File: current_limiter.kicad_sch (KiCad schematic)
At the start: 22 parts, among them J3601 Conn_02x02, Q3601 MMBT5551, Q3602 MMBT5551, Q3603 LBSS84LT1G, U3601 COS1333TR, U3602 LMV321-TR

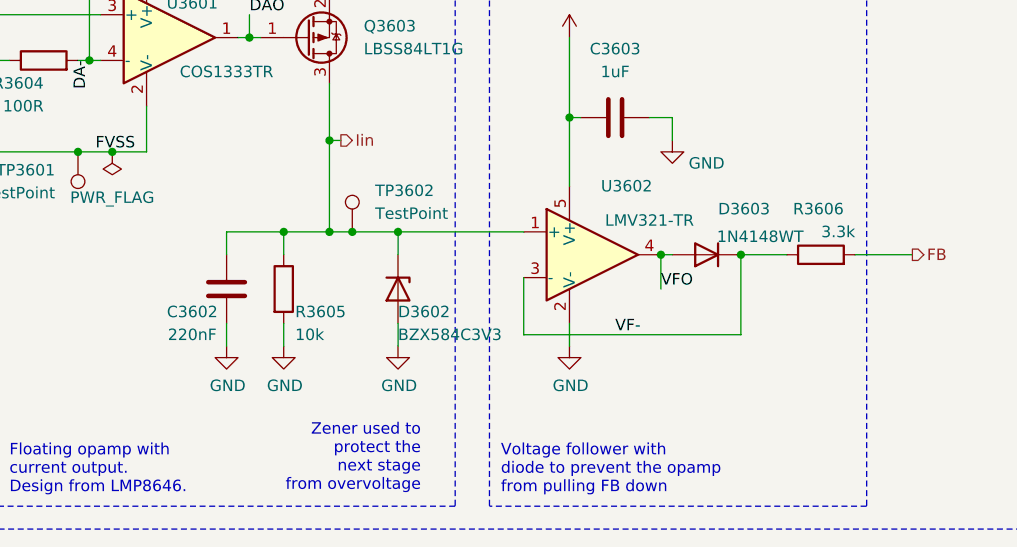
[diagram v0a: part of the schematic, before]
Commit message: Update current limiter components
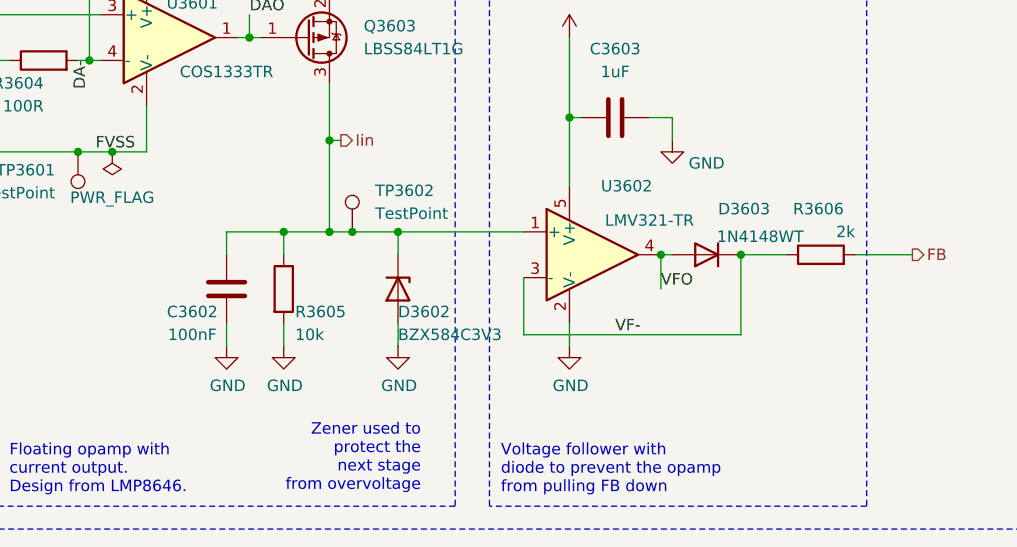
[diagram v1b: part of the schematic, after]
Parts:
- C3602: value 220nF -> 100nF; LCSC C21120 -> (none)
- R3605: footprint Resistor_SMD:R_0402_1005Metric -> Resistor_SMD:R_0603_1608Metric_Pad0.98x0.95mm_HandSolder; LCSC C25744 -> (none)
- R3606: value 3.3k -> 2k; LCSC C22978 -> (none)
- R3607: footprint Resistor_SMD:R_0402_1005Metric -> Resistor_SMD:R_0603_1608Metric_Pad0.98x0.95mm_HandSolder; LCSC C25918 -> (none)
- R3608: footprint Resistor_SMD:R_0402_1005Metric -> Resistor_SMD:R_0603_1608Metric_Pad0.98x0.95mm_HandSolder; LCSC C51721 -> (none)
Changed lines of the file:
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@@
 			)
 		)
-		(property "Footprint" "Resistor_SMD:R_0402_1005Metric"
+		(property "Footprint" "Resistor_SMD:R_0603_1608Metric_Pad0.98x0.95mm_HandSolder"
 			(at 113.792 99.06 90)
 			(effects
@@
 			)
 		)
-		(property "LCSC" "C25744"
+		(property "LCSC" ""
 			(at 115.57 99.06 0)
 			(effects
@@
 			)
 		)
-		(property "Value" "220nF"
+		(property "Value" "100nF"
 			(at 105.41 104.14 0)
 			(effects
@@
 			)
 		)
-		(property "LCSC" "C21120"
+		(property "LCSC" ""
 			(at 109.22 99.06 0)
 			(effects
@@
 			)
 		)
-		(property "Footprint" "Resistor_SMD:R_0402_1005Metric"
+		(property "Footprint" "Resistor_SMD:R_0603_1608Metric_Pad0.98x0.95mm_HandSolder"
 			(at 228.6 97.79 0)
 			(effects
@@
 			)
 		)
-		(property "LCSC" "C25918"
+		(property "LCSC" ""
 			(at 228.6 97.79 0)
 			(effects
@@
 			)
 		)
-		(property "Value" "3.3k"
+		(property "Value" "2k"
 			(at 179.07 92.71 90)
 			(effects
@@
 			)
 		)
-		(property "LCSC" "C22978"
+		(property "LCSC" ""
 			(at 175.26 95.25 0)
 			(effects
@@
 			)
 		)
-		(property "Footprint" "Resistor_SMD:R_0402_1005Metric"
+		(property "Footprint" "Resistor_SMD:R_0603_1608Metric_Pad0.98x0.95mm_HandSolder"
 			(at 241.3 97.79 0)
 			(effects
@@
 			)
 		)
-		(property "LCSC" "C51721"
+		(property "LCSC" ""
 			(at 241.3 97.79 0)
 			(effects

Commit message: Try to improve current limiter stability
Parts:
- C167: renamed from C3602; LCSC (none) -> C14663
- R116: renamed from R3605; LCSC (none) -> C25804
- R117: renamed from R3606; LCSC (none) -> C22975
- R118: renamed from R3607; LCSC (none) -> C23234
- R119: renamed from R3608; LCSC (none) -> C23018
- renumbered C3601 to C166, C3603 to C168, D3601 to D38, D3602 to D39, D3603 to D40, J3601 to J31, Q3602 to Q10, Q3603 to Q11, Q3601 to Q9, R3601 to R112, R3602 to R113, R3603 to R114, R3604 to R115, TP3601 to TP43, TP3602 to TP44, U3601 to U52, U3602 to U53

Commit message: Reannotate the board
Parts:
- renumbered C166 to C167, C167 to C168, C168 to C169, D38 to D37, D39 to D38, D40 to D39, J31 to J30, TP43 to TP42, TP44 to TP43, U52 to U51, U53 to U52
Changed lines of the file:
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@@
 		(on_board yes)
 		(dnp no)
-		(property "Reference" "J31"
+		(property "Reference" "J30"
 			(at 246.634 78.994 0)
 			(effects
@@
 			(project "HALPI2"
 				(path "/abc482bd-3f17-4d35-80db-1da3dcdb5c27/c7bf4e1f-6bd1-4be7-9e56-1bd438bf5d42/949897e8-9bb6-4c13-b9c6-3f831f2e4c69/ceedefa9-b0a1-435b-ac8f-bf0512726438"
-					(reference "J31")
+					(reference "J30")
 					(unit 1)
 				)
@@
 		(on_board yes)
 		(dnp no)
-		(property "Reference" "D40"
+		(property "Reference" "D39"
 			(at 163.83 90.17 0)
 			(effects
@@
 			(project "HALPI2"
 				(path "/abc482bd-3f17-4d35-80db-1da3dcdb5c27/c7bf4e1f-6bd1-4be7-9e56-1bd438bf5d42/949897e8-9bb6-4c13-b9c6-3f831f2e4c69/ceedefa9-b0a1-435b-ac8f-bf0512726438"
-					(reference "D40")
+					(reference "D39")
 					(unit 1)
 				)
@@
 		(dnp no)
 		(fields_autoplaced yes)
-		(property "Reference" "C168"
+		(property "Reference" "C169"
 			(at 152.4 72.39 90)
 			(effects
@@
 			(project "HALPI2"
 				(path "/abc482bd-3f17-4d35-80db-1da3dcdb5c27/c7bf4e1f-6bd1-4be7-9e56-1bd438bf5d42/949897e8-9bb6-4c13-b9c6-3f831f2e4c69/ceedefa9-b0a1-435b-ac8f-bf0512726438"
-					(reference "C168")
+					(reference "C169")
 					(unit 1)
 				)
@@
 		(dnp no)
 		(fields_autoplaced yes)
-		(property "Reference" "D38"
+		(property "Reference" "D37"
 			(at 71.12 78.7399 90)
 			(effects
@@
 			(project "HALPI2"
 				(path "/abc482bd-3f17-4d35-80db-1da3dcdb5c27/c7bf4e1f-6bd1-4be7-9e56-1bd438bf5d42/949897e8-9bb6-4c13-b9c6-3f831f2e4c69/ceedefa9-b0a1-435b-ac8f-bf0512726438"
-					(reference "D38")
+					(reference "D37")
 					(unit 1)
 				)
@@
 		(on_board yes)
 		(dnp no)
-		(property "Reference" "#PWR0324"
+		(property "Reference" "#PWR0323"
 			(at 158.75 88.9 0)
 			(effects
@@
 			(project "HALPI2"
 				(path "/abc482bd-3f17-4d35-80db-1da3dcdb5c27/c7bf4e1f-6bd1-4be7-9e56-1bd438bf5d42/949897e8-9bb6-4c13-b9c6-3f831f2e4c69/ceedefa9-b0a1-435b-ac8f-bf0512726438"
-					(reference "#PWR0324")
+					(reference "#PWR0323")
 					(unit 1)
 				)
@@
 		(on_board yes)
 		(dnp no)
-		(property "Reference" "#PWR0321"
+		(property "Reference" "#PWR0320"
 			(at 128.27 111.76 0)
 			(effects
@@
 			(project "HALPI2"
 				(path "/abc482bd-3f17-4d35-80db-1da3dcdb5c27/c7bf4e1f-6bd1-4be7-9e56-1bd438bf5d42/949897e8-9bb6-4c13-b9c6-3f831f2e4c69/ceedefa9-b0a1-435b-ac8f-bf0512726438"
-					(reference "#PWR0321")
+					(reference "#PWR0320")
 					(unit 1)
 				)
@@
 		(on_board yes)
 		(dnp no)
-		(property "Reference" "#PWR0320"
+		(property "Reference" "#PWR0319"
 			(at 115.57 111.76 0)
 			(effects
@@
 			(project "HALPI2"
 				(path "/abc482bd-3f17-4d35-80db-1da3dcdb5c27/c7bf4e1f-6bd1-4be7-9e56-1bd438bf5d42/949897e8-9bb6-4c13-b9c6-3f831f2e4c69/ceedefa9-b0a1-435b-ac8f-bf0512726438"
-					(reference "#PWR0320")
+					(reference "#PWR0319")
 					(unit 1)
 				)
@@
 		(dnp no)
 		(fields_autoplaced yes)
-		(property "Reference" "#PWR0325"
+		(property "Reference" "#PWR0324"
 			(at 228.6 111.76 0)
 			(effects
@@
 			(project "HALPI2"
 				(path "/abc482bd-3f17-4d35-80db-1da3dcdb5c27/c7bf4e1f-6bd1-4be7-9e56-1bd438bf5d42/949897e8-9bb6-4c13-b9c6-3f831f2e4c69/ceedefa9-b0a1-435b-ac8f-bf0512726438"
-					(reference "#PWR0325")
+					(reference "#PWR0324")
 					(unit 1)
 				)
@@
 		(on_board yes)
 		(dnp no)
-		(property "Reference" "C167"
+		(property "Reference" "C168"
 			(at 105.41 101.6 0)
 			(effects
@@
 			(project "HALPI2"
 				(path "/abc482bd-3f17-4d35-80db-1da3dcdb5c27/c7bf4e1f-6bd1-4be7-9e56-1bd438bf5d42/949897e8-9bb6-4c13-b9c6-3f831f2e4c69/ceedefa9-b0a1-435b-ac8f-bf0512726438"
-					(reference "C167")
+					(reference "C168")
 					(unit 1)
 				)
@@
 		(on_board yes)
 		(dnp no)
-		(property "Reference" "#PWR0323"
+		(property "Reference" "#PWR0322"
 			(at 147.32 111.76 0)
 			(effects
@@
 			(project "HALPI2"
 				(path "/abc482bd-3f17-4d35-80db-1da3dcdb5c27/c7bf4e1f-6bd1-4be7-9e56-1bd438bf5d42/949897e8-9bb6-4c13-b9c6-3f831f2e4c69/ceedefa9-b0a1-435b-ac8f-bf0512726438"
-					(reference "#PWR0323")
+					(reference "#PWR0322")
 					(unit 1)
 				)
@@
 		(dnp no)
 		(fields_autoplaced yes)
-		(property "Reference" "#PWR0326"
+		(property "Reference" "#PWR0325"
 			(at 241.3 111.76 0)
 			(effects
@@
 			(project "HALPI2"
 				(path "/abc482bd-3f17-4d35-80db-1da3dcdb5c27/c7bf4e1f-6bd1-4be7-9e56-1bd438bf5d42/949897e8-9bb6-4c13-b9c6-3f831f2e4c69/ceedefa9-b0a1-435b-ac8f-bf0512726438"
-					(reference "#PWR0326")
+					(reference "#PWR0325")
 					(unit 1)
 				)
@@
 		(on_board yes)
 		(dnp no)
-		(property "Reference" "TP43"
+		(property "Reference" "TP42"
 			(at 90.17 85.8519 0)
 			(effects
@@
 			(project "HALPI2"
 				(path "/abc482bd-3f17-4d35-80db-1da3dcdb5c27/c7bf4e1f-6bd1-4be7-9e56-1bd438bf5d42/949897e8-9bb6-4c13-b9c6-3f831f2e4c69/ceedefa9-b0a1-435b-ac8f-bf0512726438"
-					(reference "TP43")
+					(reference "TP42")
 					(unit 1)
 				)
@@
 		(on_board yes)
 		(dnp no)
-		(property "Reference" "#PWR0319"
+		(property "Reference" "#PWR0318"
 			(at 109.22 111.76 0)
 			(effects
@@
 			(project "HALPI2"
 				(path "/abc482bd-3f17-4d35-80db-1da3dcdb5c27/c7bf4e1f-6bd1-4be7-9e56-1bd438bf5d42/949897e8-9bb6-4c13-b9c6-3f831f2e4c69/ceedefa9-b0a1-435b-ac8f-bf0512726438"
-					(reference "#PWR0319")
+					(reference "#PWR0318")
 					(unit 1)
 				)
@@
 		(dnp no)
 		(fields_autoplaced yes)
-		(property "Reference" "TP44"
+		(property "Reference" "TP43"
 			(at 125.73 88.1379 0)
 			(effects
@@
 			(project "HALPI2"
 				(path "/abc482bd-3f17-4d35-80db-1da3dcdb5c27/c7bf4e1f-6bd1-4be7-9e56-1bd438bf5d42/949897e8-9bb6-4c13-b9c6-3f831f2e4c69/ceedefa9-b0a1-435b-ac8f-bf0512726438"
-					(reference "TP44")
+					(reference "TP43")
 					(unit 1)
 				)
@@
 		(dnp no)
 		(fields_autoplaced yes)
-		(property "Reference" "#FLG023"
+		(property "Reference" "#FLG022"
 			(at 91.44 55.245 0)
 			(effects
@@
 			(project "HALPI2"
 				(path "/abc482bd-3f17-4d35-80db-1da3dcdb5c27/c7bf4e1f-6bd1-4be7-9e56-1bd438bf5d42/949897e8-9bb6-4c13-b9c6-3f831f2e4c69/ceedefa9-b0a1-435b-ac8f-bf0512726438"
-					(reference "#FLG023")
+					(reference "#FLG022")
 					(unit 1)
 				)
@@
 		(dnp no)
 		(fields_autoplaced yes)
-		(property "Reference" "#PWR0322"
+		(property "Reference" "#PWR0321"
 			(at 147.32 74.93 0)
 			(effects
@@
 			(project "HALPI2"
 				(path "/abc482bd-3f17-4d35-80db-1da3dcdb5c27/c7bf4e1f-6bd1-4be7-9e56-1bd438bf5d42/949897e8-9bb6-4c13-b9c6-3f831f2e4c69/ceedefa9-b0a1-435b-ac8f-bf0512726438"
-					(reference "#PWR0322")
+					(reference "#PWR0321")
 					(unit 1)
 				)
@@
 		(on_board yes)
 		(dnp no)
-		(property "Reference" "U53"
+		(property "Reference" "U52"
 			(at 153.67 87.63 0)
 			(effects
@@
 			(project "HALPI2"
 				(path "/abc482bd-3f17-4d35-80db-1da3dcdb5c27/c7bf4e1f-6bd1-4be7-9e56-1bd438bf5d42/949897e8-9bb6-4c13-b9c6-3f831f2e4c69/ceedefa9-b0a1-435b-ac8f-bf0512726438"
-					(reference "U53")
+					(reference "U52")
 					(unit 1)
 				)
@@
 		(dnp no)
 		(fields_autoplaced yes)
-		(property "Reference" "#FLG024"
+		(property "Reference" "#FLG023"
 			(at 96.52 85.725 0)
 			(effects
@@
 			(project "HALPI2"
 				(path "/abc482bd-3f17-4d35-80db-1da3dcdb5c27/c7bf4e1f-6bd1-4be7-9e56-1bd438bf5d42/949897e8-9bb6-4c13-b9c6-3f831f2e4c69/ceedefa9-b0a1-435b-ac8f-bf0512726438"
-					(reference "#FLG024")
+					(reference "#FLG023")
 					(unit 1)
 				)
@@
 		(on_board yes)
 		(dnp no)
-		(property "Reference" "D39"
+		(property "Reference" "D38"
 			(at 128.27 101.6 90)
 			(effects
@@
 			(project "HALPI2"
 				(path "/abc482bd-3f17-4d35-80db-1da3dcdb5c27/c7bf4e1f-6bd1-4be7-9e56-1bd438bf5d42/949897e8-9bb6-4c13-b9c6-3f831f2e4c69/ceedefa9-b0a1-435b-ac8f-bf0512726438"
-					(reference "D39")
+					(reference "D38")
 					(unit 1)
 				)
@@
 		(on_board yes)
 		(dnp no)
-		(property "Reference" "#PWR0318"
+		(property "Reference" "#PWR0317"
 			(at 68.58 116.84 0)
 			(effects
@@
 			(project "HALPI2"
 				(path "/abc482bd-3f17-4d35-80db-1da3dcdb5c27/c7bf4e1f-6bd1-4be7-9e56-1bd438bf5d42/949897e8-9bb6-4c13-b9c6-3f831f2e4c69/ceedefa9-b0a1-435b-ac8f-bf0512726438"
-					(reference "#PWR0318")
+					(reference "#PWR0317")
 					(unit 1)
 				)
@@
 		(on_board yes)
 		(dnp no)
-		(property "Reference" "U52"
+		(property "Reference" "U51"
 			(at 105.41 67.31 0)
 			(effects
@@
 			(project "HALPI2"
 				(path "/abc482bd-3f17-4d35-80db-1da3dcdb5c27/c7bf4e1f-6bd1-4be7-9e56-1bd438bf5d42/949897e8-9bb6-4c13-b9c6-3f831f2e4c69/ceedefa9-b0a1-435b-ac8f-bf0512726438"
-					(reference "U52")
+					(reference "U51")
 					(unit 1)
 				)
@@
 		(on_board yes)
 		(dnp no)
-		(property "Reference" "C166"
+		(property "Reference" "C167"
 			(at 111.76 54.61 0)
 			(effects
@@
 			(project "HALPI2"
 				(path "/abc482bd-3f17-4d35-80db-1da3dcdb5c27/c7bf4e1f-6bd1-4be7-9e56-1bd438bf5d42/949897e8-9bb6-4c13-b9c6-3f831f2e4c69/ceedefa9-b0a1-435b-ac8f-bf0512726438"
-					(reference "C166")
-					(unit 1)
-				)
+					(reference "C167")
+					(unit 1)
+				)

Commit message: Fix DRC issues
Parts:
- R115: Component Class (none) -> fine_pitch

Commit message: FInal v0.2.0 proto changes
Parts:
- D37, D38, D39: JLCPCB_CORRECTION (none) -> 0;0;180
- renumbered C167 to C169, C168 to C170, C169 to C171, J30 to J35, TP42 to TP79, TP43 to TP80
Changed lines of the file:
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@@
 		(on_board yes)
 		(dnp no)
-		(property "Reference" "J30"
+		(property "Reference" "J35"
 			(at 246.634 78.994 0)
 			(effects
@@
 			(project "HALPI2"
 				(path "/abc482bd-3f17-4d35-80db-1da3dcdb5c27/c7bf4e1f-6bd1-4be7-9e56-1bd438bf5d42/949897e8-9bb6-4c13-b9c6-3f831f2e4c69/ceedefa9-b0a1-435b-ac8f-bf0512726438"
-					(reference "J30")
+					(reference "J35")
 					(unit 1)
 				)
@@
 			)
 		)
+		(property "JLCPCB_CORRECTION" "0;0;180"
+			(at 162.56 95.25 0)
+			(effects
+				(font
+					(size 1.27 1.27)
+				)
+			)
+		)
 		(pin "1"
 		)
@@
 		(dnp no)
 		(fields_autoplaced yes)
-		(property "Reference" "C169"
+		(property "Reference" "C171"
 			(at 152.4 72.39 90)
 			(effects
@@
 			(project "HALPI2"
 				(path "/abc482bd-3f17-4d35-80db-1da3dcdb5c27/c7bf4e1f-6bd1-4be7-9e56-1bd438bf5d42/949897e8-9bb6-4c13-b9c6-3f831f2e4c69/ceedefa9-b0a1-435b-ac8f-bf0512726438"
-					(reference "C169")
+					(reference "C171")
 					(unit 1)
 				)
@@
 			)
 		)
+		(property "JLCPCB_CORRECTION" "0;0;180"
+			(at 68.58 80.01 0)
+			(effects
+				(font
+					(size 1.27 1.27)
+				)
+			)
+		)
 		(pin "1"
 		)
@@
 		(on_board yes)
 		(dnp no)
-		(property "Reference" "#PWR0323"
+		(property "Reference" "#PWR0342"
 			(at 158.75 88.9 0)
 			(effects
@@
 			(project "HALPI2"
 				(path "/abc482bd-3f17-4d35-80db-1da3dcdb5c27/c7bf4e1f-6bd1-4be7-9e56-1bd438bf5d42/949897e8-9bb6-4c13-b9c6-3f831f2e4c69/ceedefa9-b0a1-435b-ac8f-bf0512726438"
-					(reference "#PWR0323")
+					(reference "#PWR0342")
 					(unit 1)
 				)
@@
 		(on_board yes)
 		(dnp no)
-		(property "Reference" "#PWR0320"
+		(property "Reference" "#PWR0339"
 			(at 128.27 111.76 0)
 			(effects
@@
 			(project "HALPI2"
 				(path "/abc482bd-3f17-4d35-80db-1da3dcdb5c27/c7bf4e1f-6bd1-4be7-9e56-1bd438bf5d42/949897e8-9bb6-4c13-b9c6-3f831f2e4c69/ceedefa9-b0a1-435b-ac8f-bf0512726438"
-					(reference "#PWR0320")
+					(reference "#PWR0339")
 					(unit 1)
 				)
@@
 		(on_board yes)
 		(dnp no)
-		(property "Reference" "#PWR0319"
+		(property "Reference" "#PWR0338"
 			(at 115.57 111.76 0)
 			(effects
@@
 			(project "HALPI2"
 				(path "/abc482bd-3f17-4d35-80db-1da3dcdb5c27/c7bf4e1f-6bd1-4be7-9e56-1bd438bf5d42/949897e8-9bb6-4c13-b9c6-3f831f2e4c69/ceedefa9-b0a1-435b-ac8f-bf0512726438"
-					(reference "#PWR0319")
+					(reference "#PWR0338")
 					(unit 1)
 				)
@@
 		(dnp no)
 		(fields_autoplaced yes)
-		(property "Reference" "#PWR0324"
+		(property "Reference" "#PWR0343"
 			(at 228.6 111.76 0)
 			(effects
@@
 			(project "HALPI2"
 				(path "/abc482bd-3f17-4d35-80db-1da3dcdb5c27/c7bf4e1f-6bd1-4be7-9e56-1bd438bf5d42/949897e8-9bb6-4c13-b9c6-3f831f2e4c69/ceedefa9-b0a1-435b-ac8f-bf0512726438"
-					(reference "#PWR0324")
+					(reference "#PWR0343")
 					(unit 1)
 				)
@@
 		(on_board yes)
 		(dnp no)
-		(property "Reference" "C168"
+		(property "Reference" "C170"
 			(at 105.41 101.6 0)
 			(effects
@@
 			(project "HALPI2"
 				(path "/abc482bd-3f17-4d35-80db-1da3dcdb5c27/c7bf4e1f-6bd1-4be7-9e56-1bd438bf5d42/949897e8-9bb6-4c13-b9c6-3f831f2e4c69/ceedefa9-b0a1-435b-ac8f-bf0512726438"
-					(reference "C168")
+					(reference "C170")
 					(unit 1)
 				)
@@
 		(on_board yes)
 		(dnp no)
-		(property "Reference" "#PWR0322"
+		(property "Reference" "#PWR0341"
 			(at 147.32 111.76 0)
 			(effects
@@
 			(project "HALPI2"
 				(path "/abc482bd-3f17-4d35-80db-1da3dcdb5c27/c7bf4e1f-6bd1-4be7-9e56-1bd438bf5d42/949897e8-9bb6-4c13-b9c6-3f831f2e4c69/ceedefa9-b0a1-435b-ac8f-bf0512726438"
-					(reference "#PWR0322")
+					(reference "#PWR0341")
 					(unit 1)
 				)
@@
 		(dnp no)
 		(fields_autoplaced yes)
-		(property "Reference" "#PWR0325"
+		(property "Reference" "#PWR0344"
 			(at 241.3 111.76 0)
 			(effects
@@
 			(project "HALPI2"
 				(path "/abc482bd-3f17-4d35-80db-1da3dcdb5c27/c7bf4e1f-6bd1-4be7-9e56-1bd438bf5d42/949897e8-9bb6-4c13-b9c6-3f831f2e4c69/ceedefa9-b0a1-435b-ac8f-bf0512726438"
-					(reference "#PWR0325")
+					(reference "#PWR0344")
 					(unit 1)
 				)
@@
 		(on_board yes)
 		(dnp no)
-		(property "Reference" "TP42"
+		(property "Reference" "TP79"
 			(at 90.17 85.8519 0)
 			(effects
@@
 			(project "HALPI2"
 				(path "/abc482bd-3f17-4d35-80db-1da3dcdb5c27/c7bf4e1f-6bd1-4be7-9e56-1bd438bf5d42/949897e8-9bb6-4c13-b9c6-3f831f2e4c69/ceedefa9-b0a1-435b-ac8f-bf0512726438"
-					(reference "TP42")
+					(reference "TP79")
 					(unit 1)
 				)
@@
 			)
 		)
-		(property "Sim.Enable" ""
-			(at 88.9 73.66 0)
+		(property "Component Class" "fine_pitch"
+			(at 88.9 73.66 90)
 			(effects
 				(font
 					(size 1.27 1.27)
 				)
+				(hide yes)
 			)
 		)
-		(property "Component Class" "fine_pitch"
-			(at 88.9 73.66 90)
+		(property "Sim.Enable" ""
+			(at 88.9 73.66 0)
 			(effects
 				(font
 					(size 1.27 1.27)
 				)
-				(hide yes)
 			)
 		)
@@
 		(on_board yes)
 		(dnp no)
-		(property "Reference" "#PWR0318"
+		(property "Reference" "#PWR0337"
 			(at 109.22 111.76 0)
 			(effects
@@
 			(project "HALPI2"
 				(path "/abc482bd-3f17-4d35-80db-1da3dcdb5c27/c7bf4e1f-6bd1-4be7-9e56-1bd438bf5d42/949897e8-9bb6-4c13-b9c6-3f831f2e4c69/ceedefa9-b0a1-435b-ac8f-bf0512726438"
-					(reference "#PWR0318")
+					(reference "#PWR0337")
 					(unit 1)
 				)
@@
 		(dnp no)
 		(fields_autoplaced yes)
-		(property "Reference" "TP43"
+		(property "Reference" "TP80"
 			(at 125.73 88.1379 0)
 			(effects
@@
 			(project "HALPI2"
 				(path "/abc482bd-3f17-4d35-80db-1da3dcdb5c27/c7bf4e1f-6bd1-4be7-9e56-1bd438bf5d42/949897e8-9bb6-4c13-b9c6-3f831f2e4c69/ceedefa9-b0a1-435b-ac8f-bf0512726438"
-					(reference "TP43")
+					(reference "TP80")
 					(unit 1)
 				)
@@
 		(dnp no)
 		(fields_autoplaced yes)
-		(property "Reference" "#PWR0321"
+		(property "Reference" "#PWR0340"
 			(at 147.32 74.93 0)
 			(effects
@@
 			(project "HALPI2"
 				(path "/abc482bd-3f17-4d35-80db-1da3dcdb5c27/c7bf4e1f-6bd1-4be7-9e56-1bd438bf5d42/949897e8-9bb6-4c13-b9c6-3f831f2e4c69/ceedefa9-b0a1-435b-ac8f-bf0512726438"
-					(reference "#PWR0321")
+					(reference "#PWR0340")
 					(unit 1)
 				)
@@
 			)
 		)
+		(property "JLCPCB_CORRECTION" "0;0;180"
+			(at 128.27 99.06 0)
+			(effects
+				(font
+					(size 1.27 1.27)
+				)
+			)
+		)
 		(pin "1"
 		)
@@
 		(on_board yes)
 		(dnp no)
-		(property "Reference" "#PWR0317"
+		(property "Reference" "#PWR0336"
 			(at 68.58 116.84 0)
 			(effects
@@
 			(project "HALPI2"
 				(path "/abc482bd-3f17-4d35-80db-1da3dcdb5c27/c7bf4e1f-6bd1-4be7-9e56-1bd438bf5d42/949897e8-9bb6-4c13-b9c6-3f831f2e4c69/ceedefa9-b0a1-435b-ac8f-bf0512726438"
-					(reference "#PWR0317")
+					(reference "#PWR0336")
 					(unit 1)
 				)
@@
 		(on_board yes)
 		(dnp no)
-		(property "Reference" "C167"
+		(property "Reference" "C169"
 			(at 111.76 54.61 0)
 			(effects
@@
 			(project "HALPI2"
 				(path "/abc482bd-3f17-4d35-80db-1da3dcdb5c27/c7bf4e1f-6bd1-4be7-9e56-1bd438bf5d42/949897e8-9bb6-4c13-b9c6-3f831f2e4c69/ceedefa9-b0a1-435b-ac8f-bf0512726438"
-					(reference "C167")
+					(reference "C169")
 					(unit 1)
 				)
